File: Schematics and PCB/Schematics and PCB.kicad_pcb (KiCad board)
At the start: 4 copper layers, 181 x 150 mm, 599 parts, among them J11 Conn_01x12, J6 UPSTREAM, J7 DOWNSTREAM_3, J8 DOWNSTREAM_1, J9 DOWNSTREAM_2, Q1 FDN340P, Q2 FDN340P, Q3 FDN340P, Q4 FS8205, SW10 1, SW100 NUMPAD15, SW101 NUMPAD16, SW102 NUMPAD17, SW103 NUMPAD18, SW104 NUMPAD19, SW105 NUMPAD20, SW108 Battery Switch, SW11 2, SW12 3, SW13 4, SW14 5, SW15 6, SW16 TAB, SW17 Q, SW18 W, SW19 E, SW2 ESC, SW20 R, SW21 T, SW22 MAYUS, SW23 A, SW24 S, SW25 D, SW26 F, SW27 G, SW28 L_SHIFT, SW29 Z, SW3 F1, SW30 X, SW31 C, SW32 V, SW33 B, SW34 L_CRTL, SW35 OS, SW36 L_ALT, SW37 L_SPACE, SW38 F7, SW39 F8, SW4 F2, SW40 F9, SW41 F10, SW42 F11, SW43 F12, SW44 PRT_SCR, SW45 DEL, SW46 7, SW47 8, SW48 9, SW49 0, SW5 F3, SW50 -, SW51 =, SW52 BACKSPACE, SW53 MACRO1, SW54 Y, SW55 U, SW56 I, SW57 O, SW58 P, SW59 [, SW6 F4, SW60 ], SW61 \, SW62 H, SW63 J, SW64 K, SW65 L, SW66 ;, SW67 ', SW68 ENTER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

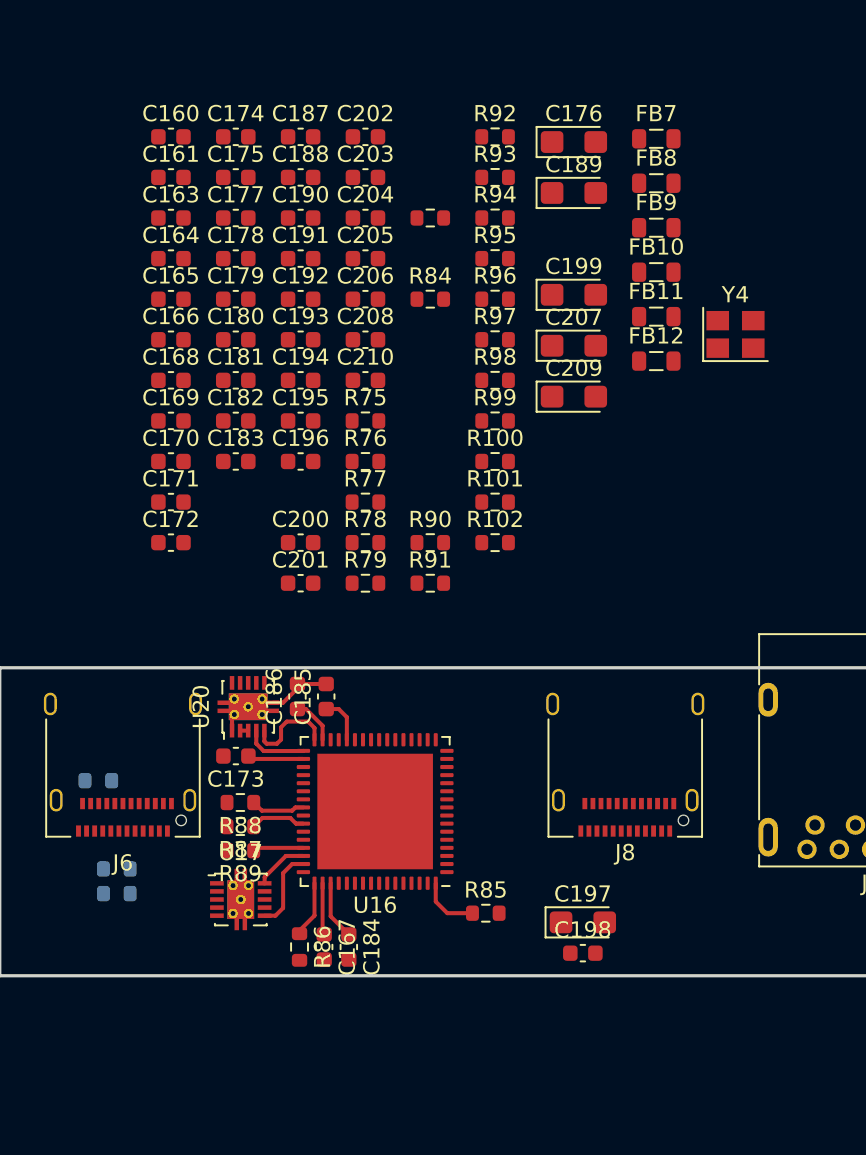
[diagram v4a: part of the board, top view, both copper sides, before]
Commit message: partially routed discrete components around hub IC
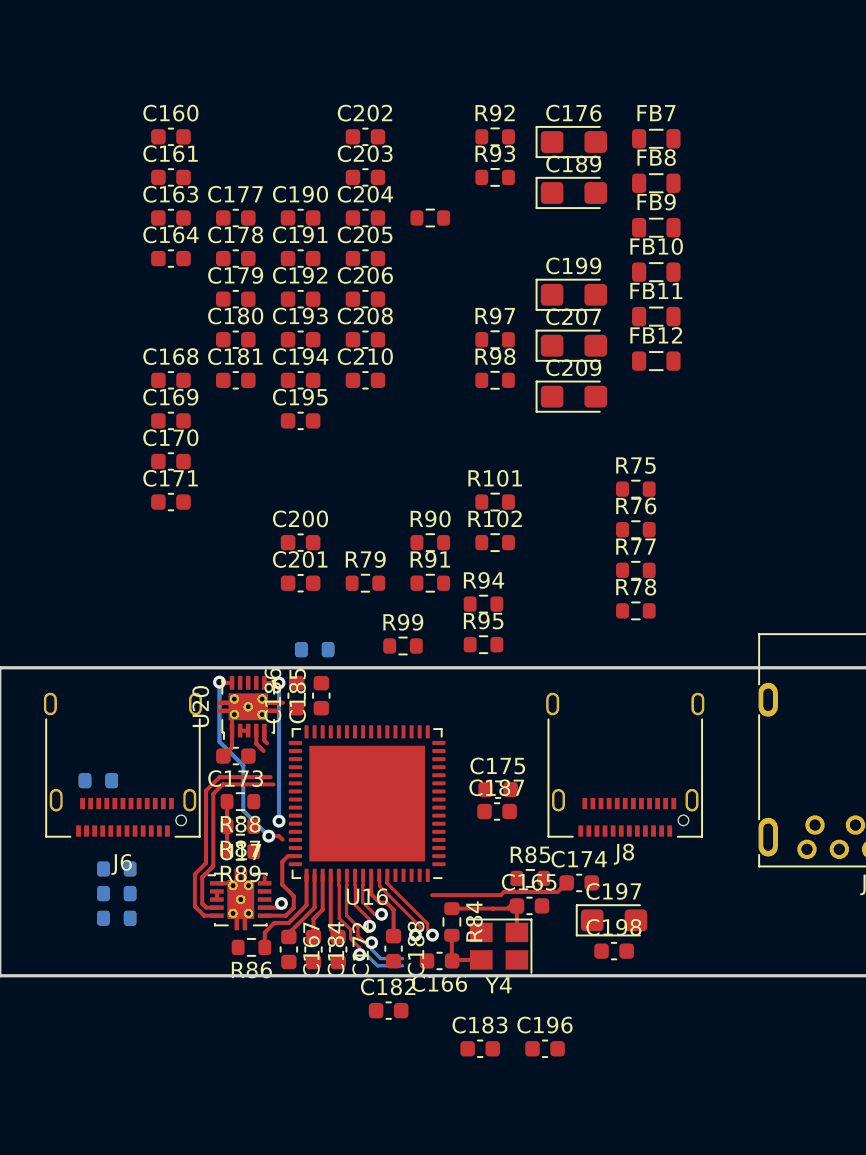
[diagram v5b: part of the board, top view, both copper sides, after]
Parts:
- R100, R96: moved to B.Cu
- moved C174 50.8 mm to (245.4, 108.6)
- moved C188 48.0 mm to (233.9, 112.6), turned to -90 degrees
- moved R96 44.9 mm to (216.8, 110.7), turned to 180 degrees
- moved C165 43.6 mm to (242.3, 110.0)
- moved C187 43.5 mm to (240.3, 104.1)
- moved C166 41.9 mm to (236.8, 113.4), turned to 180 degrees
- moved C175 41.2 mm to (240.4, 102.8)
- moved Y4 40.6 mm to (240.4, 112.5), turned to 180 degrees
- moved C183 39.3 mm to (239.3, 118.8)
- moved C196 39.3 mm to (243.3, 118.8)
- moved R84 38.5 mm to (237.5, 111.0), turned to -90 degrees
- moved C182 37.7 mm to (233.6, 116.5)
- moved C172 27.2 mm to (230.5, 112.7), turned to -90 degrees
- moved R94 23.9 mm to (239.5, 91.3)
- moved R95 23.9 mm to (239.5, 93.8)
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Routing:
- net /USB Hub/BAT_EN_2: track 0.00 -> 13.4 mm
- net /USB Hub/~{OVCURR3}: track 0.00 -> 12.5 mm, vias 0 -> 2
- net /USB Hub/BAT_EN_1: track 0.00 -> 12.1 mm
- net /USB Hub/~{OVCURR4}: track 0.00 -> 9.50 mm, vias 0 -> 2
- net +3V3: track 3.47 -> 12.9 mm
- net /USB Hub/UP_P: track 0.00 -> 8.38 mm, vias 0 -> 1
- net /USB Hub/UP_N: track 0.00 -> 7.64 mm, vias 0 -> 1
- net /USB Hub/UP_SSTX_P: track 0.00 -> 5.97 mm, vias 0 -> 1
- net /USB Hub/XI: track 0.00 -> 5.57 mm
- net /USB Hub/UP_SSTX_N: track 0.00 -> 5.22 mm, vias 0 -> 1
- net /USB Hub/BAT_EN_4: track 5.74 -> 0.86 mm
- net /USB Hub/UP_SSRX_N: track 0.00 -> 4.87 mm, vias 0 -> 1
- net /USB Hub/UP_SSRX_P: track 0.00 -> 4.87 mm, vias 0 -> 1
- net /USB Hub/XO: track 0.00 -> 3.41 mm
- net Net-(U16-FULLPWRMGMTz/SMBA1/SS_UP): track 3.36 -> 0.00 mm
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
